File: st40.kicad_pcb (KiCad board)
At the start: 2 copper layers, 228.6 x 76.2 mm, 110 parts, among them J1 USB_B_Mini, SW1 SW_SPST, SW2 SW_SPST, U1 LD1117S33TR_SOT223, U2 STM32F072CBTx

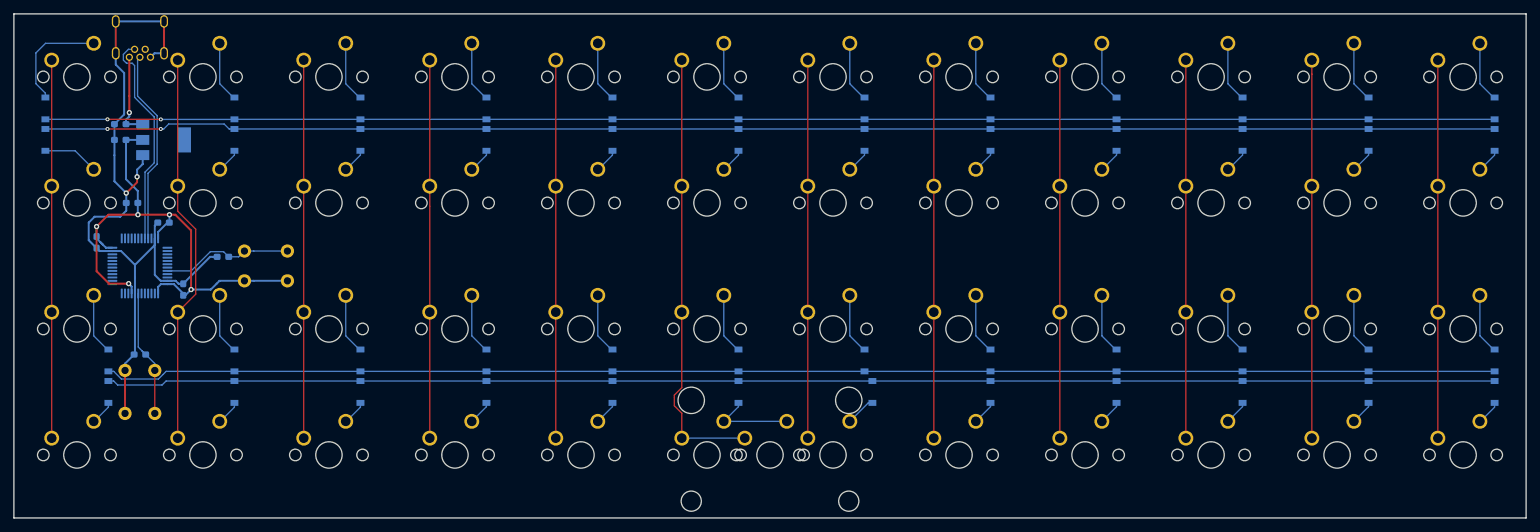
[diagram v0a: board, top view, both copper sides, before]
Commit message: fixed missing traces from col/rows to mcu, did some rerouting, fixed board outline
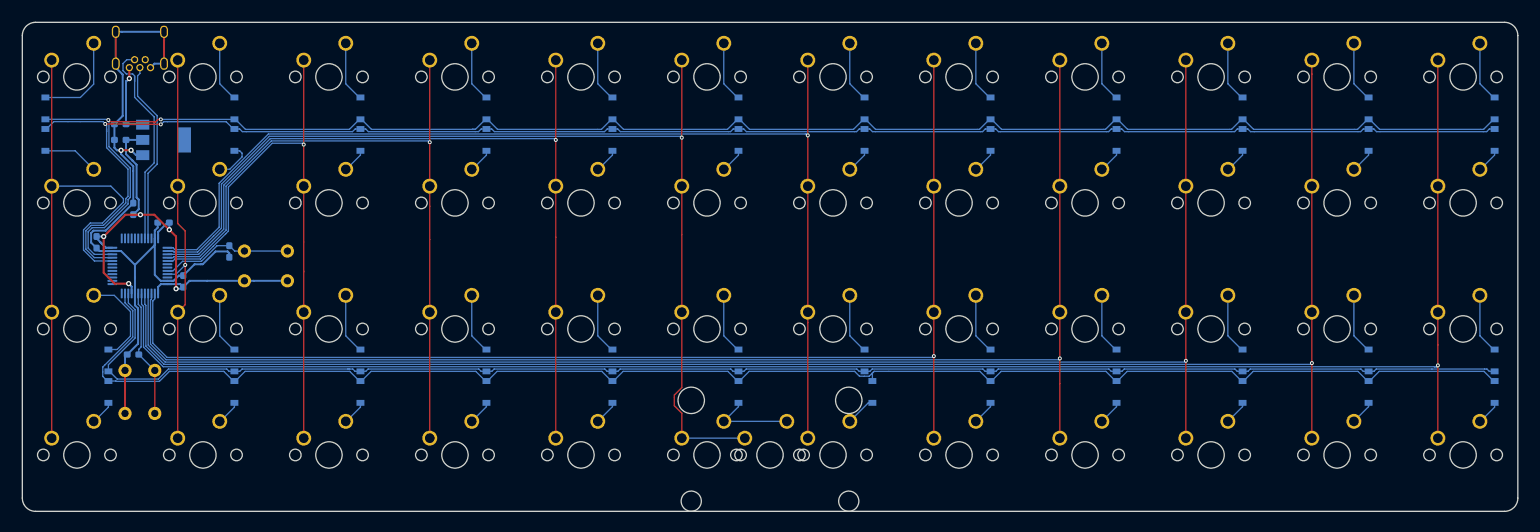
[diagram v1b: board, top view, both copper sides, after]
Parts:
- moved J1 1.57 mm to (9.53, -2.00)
- moved R1 1.26 mm to (23.0, 26.4), turned to 270 degrees
- moved C3 1.24 mm to (16.1, 30.9)
- moved C7 1.04 mm to (8.48, 42.0)
- moved C1 0.92 mm to (8.52, 19.9), turned to 90 degrees
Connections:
- U2 pad 10: Net-(U2-Pad10) -> row2
- U2 pad 11: Net-(U2-Pad11) -> row3
- U2 pad 2: Net-(U2-Pad2) -> colH
- U2 pad 20: Net-(U2-Pad20) -> colA
- U2 pad 21: Net-(U2-Pad21) -> row1
- U2 pad 22: Net-(U2-Pad22) -> row0
- U2 pad 3: Net-(U2-Pad3) -> colI
- U2 pad 37: Net-(U2-Pad37) -> colG
- U2 pad 38: Net-(U2-Pad38) -> colF
- U2 pad 39: Net-(U2-Pad39) -> colE
- U2 pad 4: Net-(U2-Pad4) -> colJ
- U2 pad 40: Net-(U2-Pad40) -> colD
- U2 pad 41: Net-(U2-Pad41) -> colC
- U2 pad 45: Net-(U2-Pad45) -> colB
- U2 pad 5: Net-(U2-Pad5) -> colK
- U2 pad 6: Net-(U2-Pad6) -> colL
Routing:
- net colL: track 57.1 -> 262.9 mm, vias 0 -> 1
- net colK: track 57.1 -> 242.7 mm, vias 0 -> 1
- net colJ: track 57.1 -> 223.0 mm, vias 0 -> 1
- net colI: track 57.1 -> 203.4 mm, vias 0 -> 1
- net colH: track 57.1 -> 183.8 mm, vias 0 -> 1
- net colG: track 57.1 -> 165.3 mm, vias 0 -> 1
- net colF: track 67.6 -> 156.6 mm, vias 0 -> 1
- net colE: track 57.1 -> 127.1 mm, vias 0 -> 1
- net colD: track 57.1 -> 108.1 mm, vias 0 -> 1
- net row0: track 219.1 -> 260.8 mm
- net row1: track 219.7 -> 252.7 mm
- net colC: track 57.1 -> 89.1 mm, vias 0 -> 1
- net row3: track 210.0 -> 239.9 mm
- net colA: track 57.1 -> 85.2 mm
- net row2: track 210.5 -> 227.8 mm
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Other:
- board size 228.6 x 76.2 mm -> 226.1 x 73.9 mm

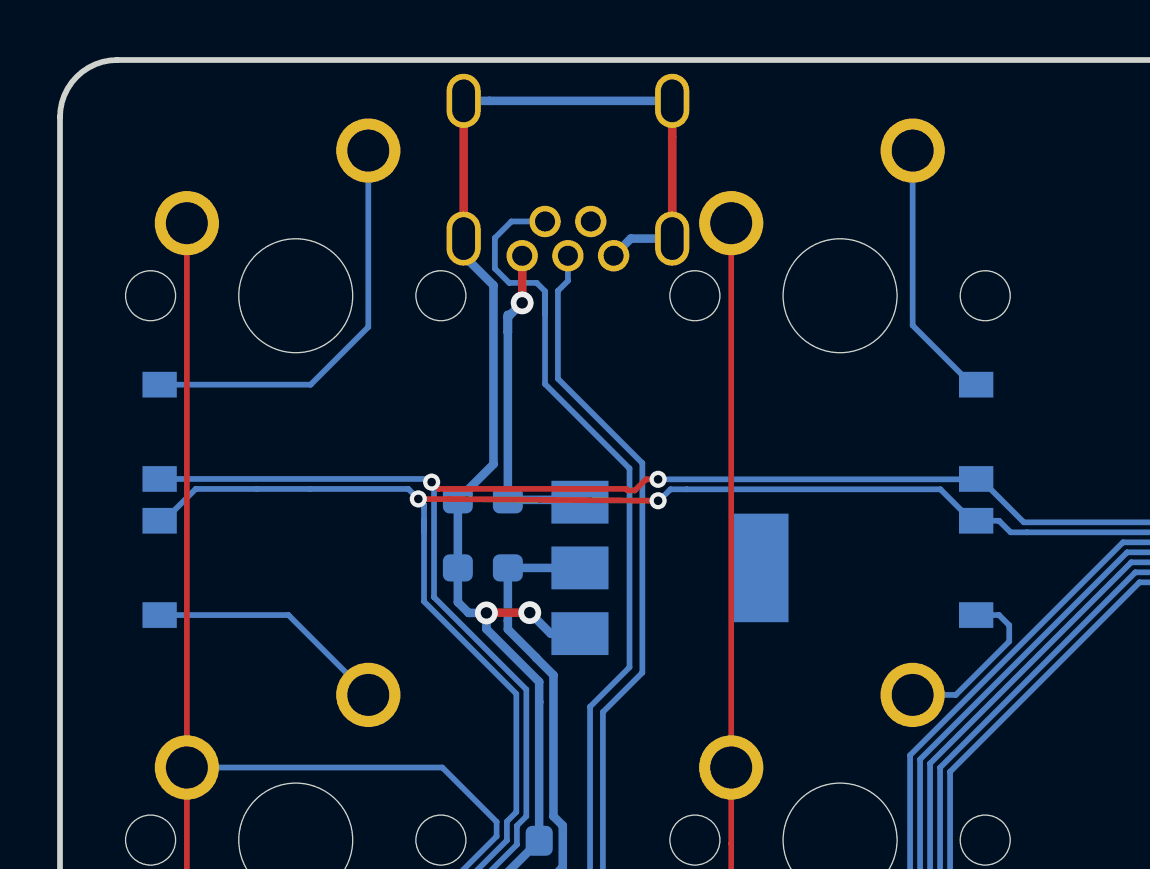
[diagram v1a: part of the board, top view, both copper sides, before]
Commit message: moved diode placement
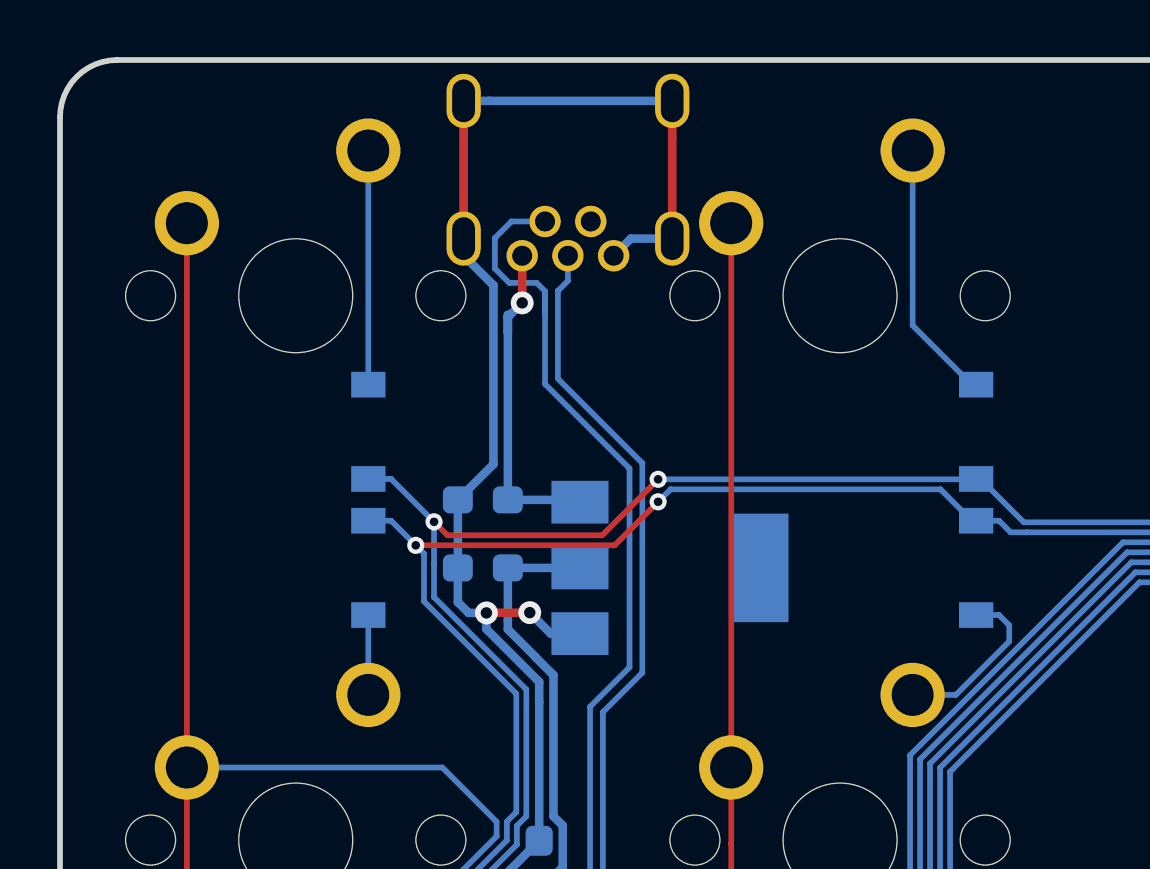
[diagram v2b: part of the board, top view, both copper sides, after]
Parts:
- moved D1 7.30 mm to (2.54, 4.76)
- moved D13 7.30 mm to (2.54, 9.53)
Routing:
- net row1: track 252.7 -> 244.0 mm
- net row0: track 260.8 -> 253.4 mm
- net Net-(D1-Pad2): track 14.3 -> 8.19 mm
- net Net-(D13-Pad2): track 8.46 -> 2.79 mm
